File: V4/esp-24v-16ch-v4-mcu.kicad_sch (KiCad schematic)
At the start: 15 parts, among them Q3 UMH3N, SW1 RESET, U3 CH340C, U4 ESP32-WROOM-32UE-N16

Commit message: Revising schematics
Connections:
- net +3.3V renamed +3V3
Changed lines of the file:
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@@
 			)
 		)
-		(property "Value" "+3.3V"
+		(property "Value" "+3V3"
 			(at 250.19 100.33 0)
 			(effects
@@
 			)
 		)
-		(property "Value" "+3.3V"
+		(property "Value" "+3V3"
 			(at 63.5 34.29 0)
 			(effects
@@
 			)
 		)
-		(property "Value" "+3.3V"
+		(property "Value" "+3V3"
 			(at 133.35 48.26 0)
 			(effects
@@
 			)
 		)
-		(property "Value" "+3.3V"
+		(property "Value" "+3V3"
 			(at 179.07 55.88 0)
 			(effects
@@
 			)
 		)
-		(property "Value" "+3.3V"
+		(property "Value" "+3V3"
 			(at 232.41 52.07 0)
 			(effects
@@
 			)
 		)
-		(property "Value" "+3.3V"
+		(property "Value" "+3V3"
 			(at 209.55 48.26 0)
 			(effects
@@
 			)
 		)
-		(property "Value" "+3.3V"
+		(property "Value" "+3V3"
 			(at 256.54 52.07 0)
 			(effects
@@
 			)
 		)
-		(property "Value" "+3.3V"
+		(property "Value" "+3V3"
 			(at 231.14 100.33 0)
 			(effects

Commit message: Revising the schematics
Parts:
- R12, R14, R19: value 10k/62,5mW -> 10k
- R13: value 22R/62,5mW -> 22R
- R15, R16, R17, R18: value 2k2/62,5mW -> 2k2
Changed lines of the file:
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@@
 			)
 		)
-		(property "Value" "22R/62,5mW"
+		(property "Value" "22R"
 			(at 208.28 88.9 90)
 			(effects
@@
 			)
 		)
-		(property "Value" "10k/62,5mW"
+		(property "Value" "10k"
 			(at 135.89 55.88 0)
 			(effects
@@
 			)
 		)
-		(property "Value" "10k/62,5mW"
+		(property "Value" "10k"
 			(at 207.01 55.88 0)
 			(effects
@@
 			)
 		)
-		(property "Value" "2k2/62,5mW"
+		(property "Value" "2k2"
 			(at 259.08 60.96 0)
 			(effects
@@
 			)
 		)
-		(property "Value" "2k2/62,5mW"
+		(property "Value" "2k2"
 			(at 252.73 109.22 0)
 			(effects
@@
 			)
 		)
-		(property "Value" "10k/62,5mW"
+		(property "Value" "10k"
 			(at 260.35 87.6299 0)
 			(effects
@@
 			)
 		)
-		(property "Value" "2k2/62,5mW"
+		(property "Value" "2k2"
 			(at 233.68 109.22 0)
 			(effects
@@
 			)
 		)
-		(property "Value" "2k2/62,5mW"
+		(property "Value" "2k2"
 			(at 234.95 60.96 0)
 			(effects

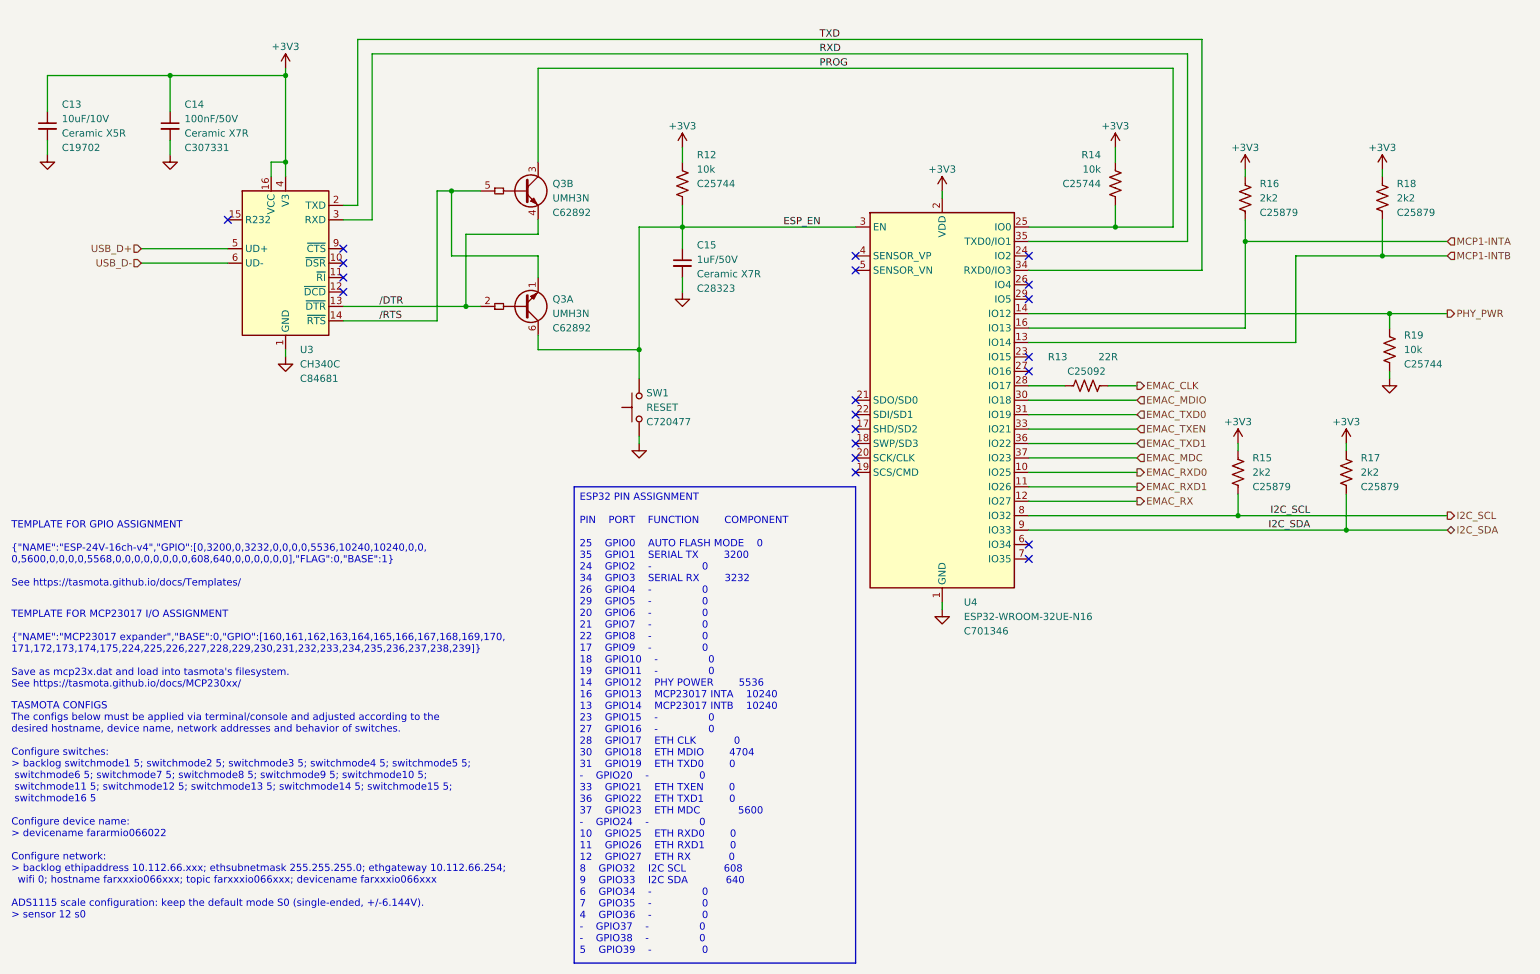
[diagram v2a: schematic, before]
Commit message: Rerouting
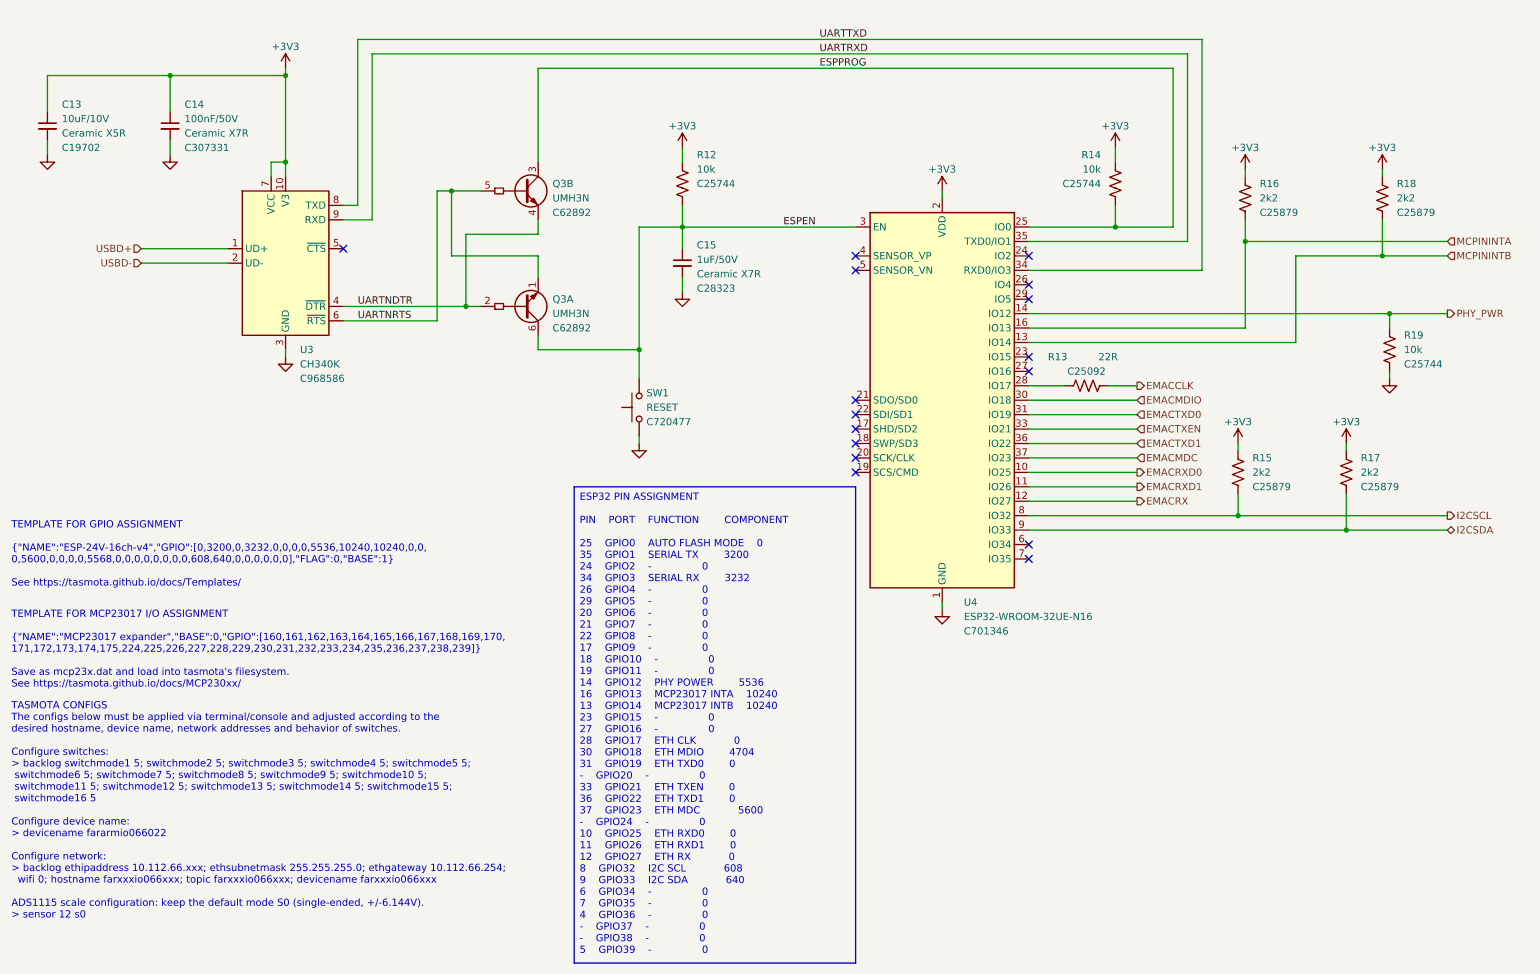
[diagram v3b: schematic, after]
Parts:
- removed U3: CH340C, Package_SO:SOIC-16_3.9x9.9mm_P1.27mm, symbol Tales:CH340C
- added U3: CH340K, Package_SO:SSOP-10-1EP_3.9x4.9mm_P1mm_EP2.1x3.3mm, symbol Interface_USB:CH340K
- R13: JLCPCB BOM (none) -> 1
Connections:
- net +3V3: now also U3.10 (V3), U3.7 (VCC)
- net GND: now also U3.11 (GND), U3.3 (GND)
- net EMAC_CLK renamed EMACCLK
- net EMAC_MDC renamed EMACMDC
- net EMAC_MDIO renamed EMACMDIO
- net EMAC_RX renamed EMACRX
- net EMAC_RXD0 renamed EMACRXD0
- net EMAC_RXD1 renamed EMACRXD1
- net EMAC_TXD0 renamed EMACTXD0
- net EMAC_TXD1 renamed EMACTXD1
- net EMAC_TXEN renamed EMACTXEN
- net ESP_EN renamed ESPEN
- net I2C_SCL renamed I2CSCL
- net I2C_SDA renamed I2CSDA
- net MCP1-INTA renamed MCPININTA
- net MCP1-INTB renamed MCPININTB
- net PROG renamed ESPPROG
- net RXD renamed UARTRXD
- net UARTRXD: now also U3.9 (RXD)
- net TXD renamed UARTTXD
- net UARTTXD: now also U3.8 (TXD)
- net /DTR renamed UARTNDTR
- net UARTNDTR: now also U3.4 (~{DTR})
- net /RTS renamed UARTNRTS
- net UARTNRTS: now also U3.6 (~{RTS})
- new net USBD+: U3.1 (UD+)
- new net USBD-: U3.2 (UD-)
- no-connect marks 20 -> 16

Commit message: Rerouting
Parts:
- added C68: 10uF/10V, Tales:C_0603_1608Metric, symbol Device:C_Small
- added C69: 100nF/50V, Tales:C_0402_1005Metric, symbol Device:C_Small
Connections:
- net +3V3: now also C68.1, C69.1
- net GND: now also C68.2, C69.2
- net ESPCLK: now reaches R13.1, U4.28 (IO17)
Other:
- moved on the sheet: R13

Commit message: Rerouting
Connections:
- net PHY_PWR renamed PHYPWR
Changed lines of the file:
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@@
 		)
 	)
-	(hierarchical_label "PHY_PWR"
+	(hierarchical_label "PHYPWR"
 		(shape output)
 		(at 267.97 81.28 0)

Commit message: Rerouting
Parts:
- R13: value 22R -> 33R; LCSC Part # C25092 -> C25105; Mfr PN 0402WGF220JTCE -> 0402WGF330JTCE; Vendor PN C25092 -> C25105
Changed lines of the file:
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@@
 	(wire
 		(pts
-			(xy 78.74 35.56) (xy 78.74 64.77)
-		)
-		(stroke
-			(width 0)
-			(type default)
-		)
-	)
-	(wire
-		(pts
-			(xy 222.25 35.56) (xy 222.25 68.58)
+			(xy 78.74 33.02) (xy 78.74 64.77)
+		)
+		(stroke
+			(width 0)
+			(type default)
+		)
+	)
+	(wire
+		(pts
+			(xy 222.25 33.02) (xy 222.25 68.58)
 		)
 		(stroke
@@
 	(wire
 		(pts
-			(xy 76.2 33.02) (xy 224.79 33.02)
+			(xy 76.2 30.48) (xy 224.79 30.48)
 		)
 		(stroke
@@
 	(wire
 		(pts
-			(xy 76.2 62.23) (xy 76.2 33.02)
+			(xy 76.2 62.23) (xy 76.2 30.48)
 		)
 		(stroke
@@
 	(wire
 		(pts
-			(xy 224.79 33.02) (xy 224.79 73.66)
+			(xy 224.79 30.48) (xy 224.79 73.66)
 		)
 		(stroke
@@
 	(wire
 		(pts
-			(xy 78.74 35.56) (xy 222.25 35.56)
+			(xy 78.74 33.02) (xy 222.25 33.02)
 		)
 		(stroke
@@
 	)
 	(label "UARTTXD"
-		(at 157.48 33.02 0)
+		(at 157.48 30.48 0)
 		(effects
 			(font
@@
 	)
 	(label "UARTRXD"
-		(at 157.48 35.56 0)
+		(at 157.48 33.02 0)
 		(effects
 			(font
@@
 			)
 		)
-		(property "Value" "22R"
+		(property "Value" "33R"
 			(at 212.09 88.9 90)
 			(effects
@@
 			)
 		)
-		(property "LCSC Part #" "C25092"
+		(property "LCSC Part #" "C25105"
 			(at 208.28 91.44 90)
 			(effects
@@
 			)
 		)
-		(property "Mfr PN" "0402WGF220JTCE"
+		(property "Mfr PN" "0402WGF330JTCE"
 			(at 208.28 93.98 0)
 			(effects
@@
 			)
 		)
-		(property "Vendor PN" "C25092"
+		(property "Vendor PN" "C25105"
 			(at 208.28 93.98 0)
 			(effects

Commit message: Rerouting
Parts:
- renumbered C68 to C16, C69 to C17, R14 to R13, R16 to R14, R18 to R15, R19 to R16, R13 to R17, R15 to R18, R17 to R19
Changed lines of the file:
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@@
 		(on_board yes)
 		(dnp no)
-		(property "Reference" "#PWR040"
+		(property "Reference" "#PWR0196"
 			(at 250.19 107.95 0)
 			(effects
@@
 			(project "esp-24v-16ch-v4"
 				(path "/2bc5a21a-1d79-419d-a592-6852cc07b00a/f2a42251-1da5-495a-abaf-29698c5bb0fe"
-					(reference "#PWR040")
+					(reference "#PWR0196")
 					(unit 1)
 				)
@@
 		(on_board yes)
 		(dnp no)
-		(property "Reference" "R13"
+		(property "Reference" "R17"
 			(at 203.2 88.9 90)
 			(effects
@@
 			(project ""
 				(path "/2bc5a21a-1d79-419d-a592-6852cc07b00a/f2a42251-1da5-495a-abaf-29698c5bb0fe"
-					(reference "R13")
+					(reference "R17")
 					(unit 1)
 				)
@@
 		(on_board yes)
 		(dnp no)
-		(property "Reference" "R14"
+		(property "Reference" "R13"
 			(at 207.01 53.34 0)
 			(effects
@@
 			(project "esp-24v-16ch-v4"
 				(path "/2bc5a21a-1d79-419d-a592-6852cc07b00a/f2a42251-1da5-495a-abaf-29698c5bb0fe"
-					(reference "R14")
+					(reference "R13")
 					(unit 1)
 				)
@@
 		(on_board yes)
 		(dnp no)
-		(property "Reference" "C69"
+		(property "Reference" "C17"
 			(at 185.42 50.8 0)
 			(effects
@@
 			(project "esp-24v-16ch-v4"
 				(path "/2bc5a21a-1d79-419d-a592-6852cc07b00a/f2a42251-1da5-495a-abaf-29698c5bb0fe"
-					(reference "C69")
+					(reference "C17")
 					(unit 1)
 				)
@@
 		(dnp no)
 		(fields_autoplaced yes)
-		(property "Reference" "#PWR0250"
+		(property "Reference" "#PWR0201"
 			(at 182.88 63.5 0)
 			(effects
@@
 			(project "esp-24v-16ch-v4"
 				(path "/2bc5a21a-1d79-419d-a592-6852cc07b00a/f2a42251-1da5-495a-abaf-29698c5bb0fe"
-					(reference "#PWR0250")
+					(reference "#PWR0201")
 					(unit 1)
 				)
@@
 		(dnp no)
 		(fields_autoplaced yes)
-		(property "Reference" "#PWR029"
+		(property "Reference" "#PWR0204"
 			(at 43.18 59.69 0)
 			(effects
@@
 			(project "esp-24v-16ch-v4"
 				(path "/2bc5a21a-1d79-419d-a592-6852cc07b00a/f2a42251-1da5-495a-abaf-29698c5bb0fe"
-					(reference "#PWR029")
+					(reference "#PWR0204")
 					(unit 1)
 				)
@@
 		(on_board yes)
 		(dnp no)
-		(property "Reference" "R18"
+		(property "Reference" "R15"
 			(at 259.08 58.42 0)
 			(effects
@@
 			(project "esp-24v-16ch-v4"
 				(path "/2bc5a21a-1d79-419d-a592-6852cc07b00a/f2a42251-1da5-495a-abaf-29698c5bb0fe"
-					(reference "R18")
+					(reference "R15")
 					(unit 1)
 				)
@@
 		(dnp no)
 		(fields_autoplaced yes)
-		(property "Reference" "#PWR0248"
+		(property "Reference" "#PWR0191"
 			(at 160.02 63.5 0)
 			(effects
@@
 			(project "esp-24v-16ch-v4"
 				(path "/2bc5a21a-1d79-419d-a592-6852cc07b00a/f2a42251-1da5-495a-abaf-29698c5bb0fe"
-					(reference "#PWR0248")
+					(reference "#PWR0191")
 					(unit 1)
 				)
@@
 		(dnp no)
 		(fields_autoplaced yes)
-		(property "Reference" "#PWR042"
+		(property "Reference" "#PWR0195"
 			(at 257.81 99.06 0)
 			(effects
@@
 			(project "esp-24v-16ch-v4"
 				(path "/2bc5a21a-1d79-419d-a592-6852cc07b00a/f2a42251-1da5-495a-abaf-29698c5bb0fe"
-					(reference "#PWR042")
+					(reference "#PWR0195")
 					(unit 1)
 				)
@@
 		(on_board yes)
 		(dnp no)
-		(property "Reference" "R17"
+		(property "Reference" "R19"
 			(at 252.73 106.68 0)
 			(effects
@@
 			(project "esp-24v-16ch-v4"
 				(path "/2bc5a21a-1d79-419d-a592-6852cc07b00a/f2a42251-1da5-495a-abaf-29698c5bb0fe"
-					(reference "R17")
+					(reference "R19")
 					(unit 1)
 				)
@@
 		(dnp no)
 		(fields_autoplaced yes)
-		(property "Reference" "#PWR028"
+		(property "Reference" "#PWR0205"
 			(at 21.59 59.69 0)
 			(effects
@@
 			(project "esp-24v-16ch-v4"
 				(path "/2bc5a21a-1d79-419d-a592-6852cc07b00a/f2a42251-1da5-495a-abaf-29698c5bb0fe"
-					(reference "#PWR028")
+					(reference "#PWR0205")
 					(unit 1)
 				)
@@
 		(on_board yes)
 		(dnp no)
-		(property "Reference" "#PWR030"
+		(property "Reference" "#PWR0202"
 			(at 63.5 41.91 0)
 			(effects
@@
 			(project "esp-24v-16ch-v4"
 				(path "/2bc5a21a-1d79-419d-a592-6852cc07b00a/f2a42251-1da5-495a-abaf-29698c5bb0fe"
-					(reference "#PWR030")
+					(reference "#PWR0202")
 					(unit 1)
 				)
@@
 		(on_board yes)
 		(dnp no)
-		(property "Reference" "#PWR033"
+		(property "Reference" "#PWR0193"
 			(at 133.35 55.88 0)
 			(effects
@@
 			(project "esp-24v-16ch-v4"
 				(path "/2bc5a21a-1d79-419d-a592-6852cc07b00a/f2a42251-1da5-495a-abaf-29698c5bb0fe"
-					(reference "#PWR033")
+					(reference "#PWR0193")
 					(unit 1)
 				)
@@
 		(dnp no)
 		(fields_autoplaced yes)
-		(property "Reference" "#PWR031"
+		(property "Reference" "#PWR0203"
 			(at 63.5 95.25 0)
 			(effects
@@
 			(project "esp-24v-16ch-v4"
 				(path "/2bc5a21a-1d79-419d-a592-6852cc07b00a/f2a42251-1da5-495a-abaf-29698c5bb0fe"
-					(reference "#PWR031")
+					(reference "#PWR0203")
 					(unit 1)
 				)
@@
 		(dnp no)
 		(fields_autoplaced yes)
-		(property "Reference" "R19"
+		(property "Reference" "R16"
 			(at 260.35 85.0899 0)
 			(effects
@@
 			(project "esp-24v-16ch-v4"
 				(path "/2bc5a21a-1d79-419d-a592-6852cc07b00a/f2a42251-1da5-495a-abaf-29698c5bb0fe"
-					(reference "R19")
+					(reference "R16")
 					(unit 1)
 				)
@@
 		(on_board yes)
 		(dnp no)
-		(property "Reference" "R15"
+		(property "Reference" "R18"
 			(at 233.68 106.68 0)
 			(effects
@@
 			(project "esp-24v-16ch-v4"
 				(path "/2bc5a21a-1d79-419d-a592-6852cc07b00a/f2a42251-1da5-495a-abaf-29698c5bb0fe"
-					(reference "R15")
+					(reference "R18")
 					(unit 1)
 				)
@@
 		(on_board yes)
 		(dnp no)
-		(property "Reference" "R16"
+		(property "Reference" "R14"
 			(at 234.95 58.42 0)
 			(effects
@@
 			(project "esp-24v-16ch-v4"
 				(path "/2bc5a21a-1d79-419d-a592-6852cc07b00a/f2a42251-1da5-495a-abaf-29698c5bb0fe"
-					(reference "R16")
+					(reference "R14")
 					(unit 1)
 				)
@@
 		(on_board yes)
 		(dnp no)
-		(property "Reference" "C68"
+		(property "Reference" "C16"
 			(at 162.56 51.435 0)
 			(effects
@@
 			(project "esp-24v-16ch-v4"
 				(path "/2bc5a21a-1d79-419d-a592-6852cc07b00a/f2a42251-1da5-495a-abaf-29698c5bb0fe"
-					(reference "C68")
+					(reference "C16")
 					(unit 1)
 				)
@@
 		(fields_autoplaced yes)
 		(property "Reference" "C15"
-			(at 135.89 69.2213 0)
+			(at 135.89 68.5862 0)
 			(effects
 				(font
@@
 		)
 		(property "Value" "1uF/50V"
-			(at 135.89 71.7613 0)
+			(at 135.89 71.1262 0)
 			(effects
 				(font
@@
 		)
 		(property "Technology" "Ceramic X7R"
-			(at 135.89 74.3013 0)
+			(at 135.89 73.6662 0)
 			(effects
 				(font
@@
 		)
 		(property "LCSC Part #" "C28323"
-			(at 135.89 76.8413 0)
+			(at 135.89 76.2062 0)
 			(effects
 				(font
@@
 		(on_board yes)
 		(dnp no)
-		(property "Reference" "#PWR035"
+		(property "Reference" "#PWR0192"
 			(at 179.07 50.8 0)
 			(effects
@@
 			(project "esp-24v-16ch-v4"
 				(path "/2bc5a21a-1d79-419d-a592-6852cc07b00a/f2a42251-1da5-495a-abaf-29698c5bb0fe"
-					(reference "#PWR035")
+					(reference "#PWR0192")
 					(unit 1)
 				)
@@
 		(dnp no)
 		(fields_autoplaced yes)
-		(property "Reference" "#PWR032"
+		(property "Reference" "#PWR0189"
 			(at 125.73 110.49 0)
 			(effects
@@
 			(project "esp-24v-16ch-v4"
 				(path "/2bc5a21a-1d79-419d-a592-6852cc07b00a/f2a42251-1da5-495a-abaf-29698c5bb0fe"
-					(reference "#PWR032")
+					(reference "#PWR0189")
 					(unit 1)
 				)
@@
 		(on_board yes)
 		(dnp no)
-		(property "Reference" "#PWR039"
+		(property "Reference" "#PWR0198"
 			(at 232.41 59.69 0)
 			(effects
@@
 			(project "esp-24v-16ch-v4"
 				(path "/2bc5a21a-1d79-419d-a592-6852cc07b00a/f2a42251-1da5-495a-abaf-29698c5bb0fe"
-					(reference "#PWR039")
+					(reference "#PWR0198")
 					(unit 1)
 				)
@@
 		(dnp no)
 		(fields_autoplaced yes)
-		(property "Reference" "#PWR034"
+		(property "Reference" "#PWR0190"
 			(at 133.35 83.82 0)
 			(effects
@@
 			(project "esp-24v-16ch-v4"
 				(path "/2bc5a21a-1d79-419d-a592-6852cc07b00a/f2a42251-1da5-495a-abaf-29698c5bb0fe"
-					(reference "#PWR034")
+					(reference "#PWR0190")
 					(unit 1)
 				)
@@
 		(dnp no)
 		(fields_autoplaced yes)
-		(property "Reference" "#PWR036"
+		(property "Reference" "#PWR0199"
 			(at 179.07 139.7 0)
 			(effects
@@
 			(project "esp-24v-16ch-v4"
 				(path "/2bc5a21a-1d79-419d-a592-6852cc07b00a/f2a42251-1da5-495a-abaf-29698c5bb0fe"
-					(reference "#PWR036")
+					(reference "#PWR0199")
 					(unit 1)
 				)
@@
 		(on_board yes)
 		(dnp no)
-		(property "Reference" "#PWR037"
+		(property "Reference" "#PWR0200"
 			(at 209.55 55.88 0)
 			(effects
@@
 			(project "esp-24v-16ch-v4"
 				(path "/2bc5a21a-1d79-419d-a592-6852cc07b00a/f2a42251-1da5-495a-abaf-29698c5bb0fe"
-					(reference "#PWR037")
+					(reference "#PWR0200")
 					(unit 1)
 				)
@@
 		(on_board yes)
 		(dnp no)
-		(property "Reference" "#PWR041"
+		(property "Reference" "#PWR0197"
 			(at 256.54 59.69 0)
 			(effects
@@
 			(project "esp-24v-16ch-v4"
 				(path "/2bc5a21a-1d79-419d-a592-6852cc07b00a/f2a42251-1da5-495a-abaf-29698c5bb0fe"
-					(reference "#PWR041")
+					(reference "#PWR0197")
 					(unit 1)
 				)
@@
 		(on_board yes)
 		(dnp no)
-		(property "Reference" "#PWR038"
+		(property "Reference" "#PWR0194"
 			(at 231.14 107.95 0)
 			(effects
@@
 			(project "esp-24v-16ch-v4"
 				(path "/2bc5a21a-1d79-419d-a592-6852cc07b00a/f2a42251-1da5-495a-abaf-29698c5bb0fe"
-					(reference "#PWR038")
+					(reference "#PWR0194")
 					(unit 1)
 				)
